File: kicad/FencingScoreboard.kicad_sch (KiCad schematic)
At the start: 6 parts, among them IC1 PIC16F18855-I-ML, J1 USB_B_Micro

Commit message: Schematic design
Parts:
- added BZ1: Buzzer, symbol Device:Buzzer
- added C1, C2, C3: 100nF, Capacitor_SMD:C_0603_1608Metric, symbol Device:C
- added ICSP: Conn_01x06_Socket, Connector_PinHeader_2.54mm:PinHeader_1x06_P2.54mm_Vertical, symbol Connector:Conn_01x06_Socket
- added J2: Conn_01x04_Socket, Connector_PinHeader_2.54mm:PinHeader_1x04_P2.54mm_Vertical, symbol Connector:Conn_01x04_Socket
- added Q1: 2N7002, Package_TO_SOT_SMD:SOT-23, symbol Transistor_FET:2N7002
- added R1: 10K, Resistor_SMD:R_0805_2012Metric, symbol Device:R
- added R2, R3: 3K6, Resistor_SMD:R_0805_2012Metric, symbol Device:R
- added R4: 1K, Resistor_SMD:R_0805_2012Metric, symbol Device:R
- IC1: footprint (none) -> Package_DFN_QFN:QFN-28-1EP_6x6mm_P0.65mm_EP4.25x4.25mm_ThermalVias
- IC2: value ~ -> TLC59281RGE
- IC3: value ~ -> TLC59281RGE; footprint (none) -> Package_DFN_QFN:QFN-28-1EP_6x6mm_P0.65mm_EP4.25x4.25mm
- J1: footprint (none) -> DMW-Custom:Molex_105164-0001_MicroUSB
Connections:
- net +5V: now also D1.18 (D3+), D1.19 (D2+), D1.26 (D1+), D2.18 (D3+), D2.19 (D2+), D2.26 (D1+), IC1.17 (VDD), IC2.21 (VCC), IC3.21 (VCC), J1.1 (VBUS), C1.1, C2.1, C3.1, ICSP.2 (Pin_2), Q1.3 (D), R1.2
- net GND: now also IC1.16 (VSS), IC1.5 (VSS), IC2.22 (GND), IC3.22 (GND), J1.5 (GND), J1.6 (Shield), BZ1.2 (+), C1.2, C2.2, C3.2, ICSP.3 (Pin_3), R2.2, R3.2, R4.1
- net at D1.11 (D3D-): now also IC2.13 (OUT11)
- net at D1.12 (D3G-): now also IC2.14 (OUT12)
- net at D1.16 (D3A-): now also IC2.12 (OUT10)
- net at D1.2 (D1D-): now also IC2.10 (OUT8)
- net at D1.20 (D2B-): now also IC2.3 (OUT1)
- net at D1.21 (D2A-): now also IC2.2 (OUT0)
- net at D1.22 (D2G-): now also IC2.8 (OUT6)
- net at D1.23 (D2F-): now also IC2.7 (OUT5)
- net at D1.25 (D1A-): now also IC2.9 (OUT7)
- net at D1.28 (D1G-): now also IC2.11 (OUT9)
- net at D1.6 (D2E-): now also IC2.6 (OUT4)
- net at D1.7 (D2D-): now also IC2.5 (OUT3)
- net at D1.8 (D2C-): now also IC2.4 (OUT2)
- net at D2.11 (D3D-): now also IC3.13 (OUT11)
- net at D2.12 (D3G-): now also IC3.14 (OUT12)
- net at D2.16 (D3A-): now also IC3.12 (OUT10)
- net at D2.2 (D1D-): now also IC3.10 (OUT8)
- net at D2.20 (D2B-): now also IC3.3 (OUT1)
- net at D2.21 (D2A-): now also IC3.2 (OUT0)
- net at D2.22 (D2G-): now also IC3.8 (OUT6)
- net at D2.23 (D2F-): now also IC3.7 (OUT5)
- net at D2.25 (D1A-): now also IC3.9 (OUT7)
- net at D2.28 (D1G-): now also IC3.11 (OUT9)
- net at D2.6 (D2E-): now also IC3.6 (OUT4)
- net at D2.7 (D2D-): now also IC3.5 (OUT3)
- net at D2.8 (D2C-): now also IC3.4 (OUT2)
- net at IC1.1 (RA2): now also IC2.1 (LAT)
- net at IC1.10 (RC2): now also J2.3 (Pin_3)
- net at IC1.11 (RC3): now also J2.4 (Pin_4)
- net at IC1.18 (RB0): now also Q1.1 (G)
- net at IC1.2 (RA3): now also IC3.1 (LAT)
- net at IC1.24 (ICSPCLK/RB6): now also ICSP.5 (Pin_5)
- net at IC1.25 (ISCPDAT/RB7): now also ICSP.4 (Pin_4)
- net at IC1.26 (RE3/~{MCLR}/VPP): now also ICSP.1 (Pin_1), R1.1
- net at IC1.27 (RA0): now also IC2.24 (SCLK), IC3.24 (SCLK)
- net at IC1.28 (RA1): now also IC2.23 (SIN), IC3.23 (SIN)
- net at IC1.8 (RC0): now also J2.1 (Pin_1)
- net at IC1.9 (RC1): now also J2.2 (Pin_2)
- net at IC2.20 (IREF): now also R2.1
- net at IC3.20 (IREF): now also R3.1
- new net: BZ1.1 (-), Q1.2 (S), R4.2

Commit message: PCB development
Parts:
- BZ1: footprint (none) -> Buzzer_Beeper:Buzzer_12x9.5RM7.6
- D1, D2: footprint (none) -> DMW-Custom:LDT-x51xRI
- IC2: footprint (none) -> Package_DFN_QFN:QFN-24-1EP_4x4mm_P0.5mm_EP2.15x2.15mm_ThermalVias
- IC3: footprint Package_DFN_QFN:QFN-28-1EP_6x6mm_P0.65mm_EP4.25x4.25mm -> Package_DFN_QFN:QFN-24-1EP_4x4mm_P0.5mm_EP2.15x2.15mm_ThermalVias
- renumbered ICSP to ICSP1
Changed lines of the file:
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@@
       (effects (font (size 1.524 1.524)))
     )
-    (property "Footprint" "" (at 138.43 143.51 0)
+    (property "Footprint" "DMW-Custom:LDT-x51xRI" (at 138.43 143.51 0)
       (effects (font (size 1.524 1.524)))
     )
@@
       (effects (font (size 1.27 1.27)))
     )
-    (property "Footprint" "Package_DFN_QFN:QFN-28-1EP_6x6mm_P0.65mm_EP4.25x4.25mm" (at 172.72 157.48 0)
+    (property "Footprint" "Package_DFN_QFN:QFN-24-1EP_4x4mm_P0.5mm_EP2.15x2.15mm_ThermalVias" (at 172.72 157.48 0)
       (effects (font (size 1.27 1.27)) hide)
     )
@@
   (symbol (lib_id "Connector:Conn_01x06_Socket") (at 146.05 76.2 0) (unit 1)
     (in_bom yes) (on_board yes) (dnp no)
-    (property "Reference" "ICSP" (at 146.05 68.58 0)
+    (property "Reference" "ICSP1" (at 146.05 68.58 0)
       (effects (font (size 1.27 1.27)))
     )
@@
       (project "FencingScoreboard"
         (path "/ffddfb19-0df0-46d6-bd3f-7efd29422964"
-          (reference "ICSP") (unit 1)
+          (reference "ICSP1") (unit 1)
         )
       )
@@
       (effects (font (size 1.524 1.524)))
     )
-    (property "Footprint" "" (at 38.1 166.37 0)
+    (property "Footprint" "DMW-Custom:LDT-x51xRI" (at 38.1 166.37 0)
       (effects (font (size 1.524 1.524)))
     )
@@
       (effects (font (size 1.27 1.27)))
     )
-    (property "Footprint" "" (at 66.04 187.96 0)
+    (property "Footprint" "Package_DFN_QFN:QFN-24-1EP_4x4mm_P0.5mm_EP2.15x2.15mm_ThermalVias" (at 66.04 187.96 0)
       (effects (font (size 1.27 1.27)) hide)
     )
@@
       (effects (font (size 1.27 1.27)) (justify left))
     )
-    (property "Footprint" "" (at 163.195 55.88 90)
-      (effects (font (size 1.27 1.27)) hide)
-    )
+    (property "Footprint" "Buzzer_Beeper:Buzzer_12x9.5RM7.6" (at 163.195 55.88 90)
+      (effects (font (size 1.27 1.27)) hide)
+    )

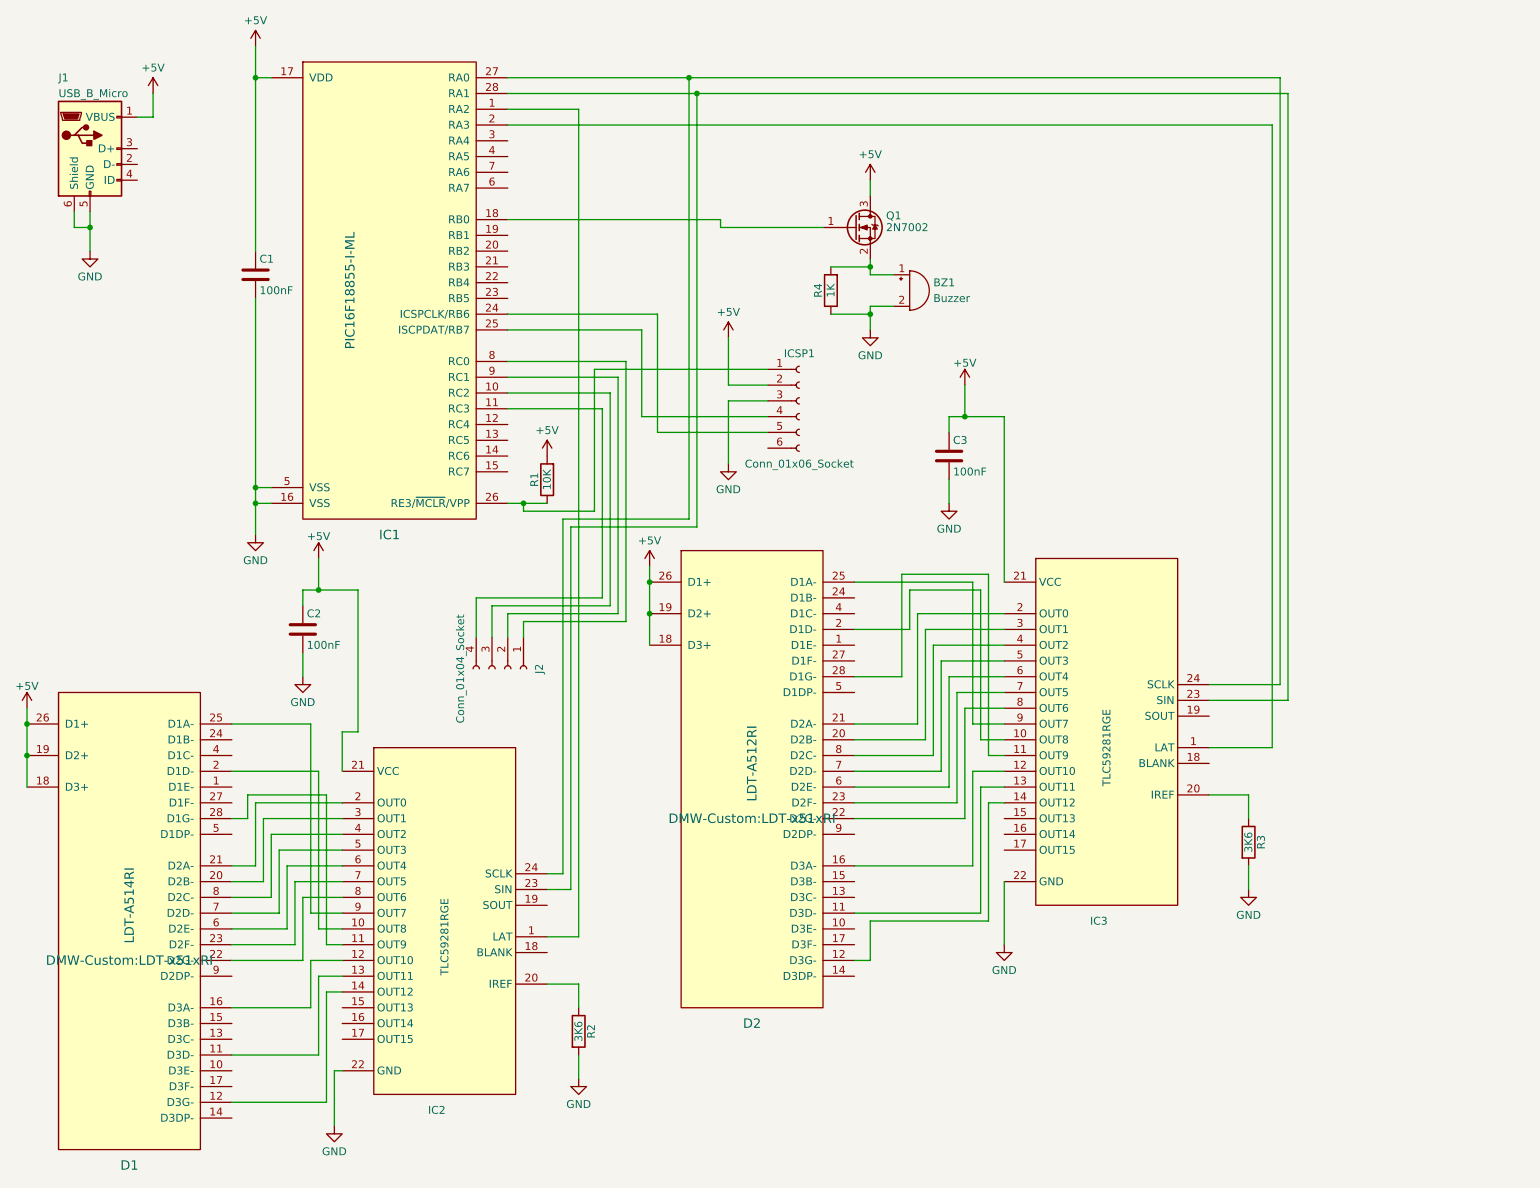
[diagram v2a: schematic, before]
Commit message: Redesign for new LED driver, route PCB
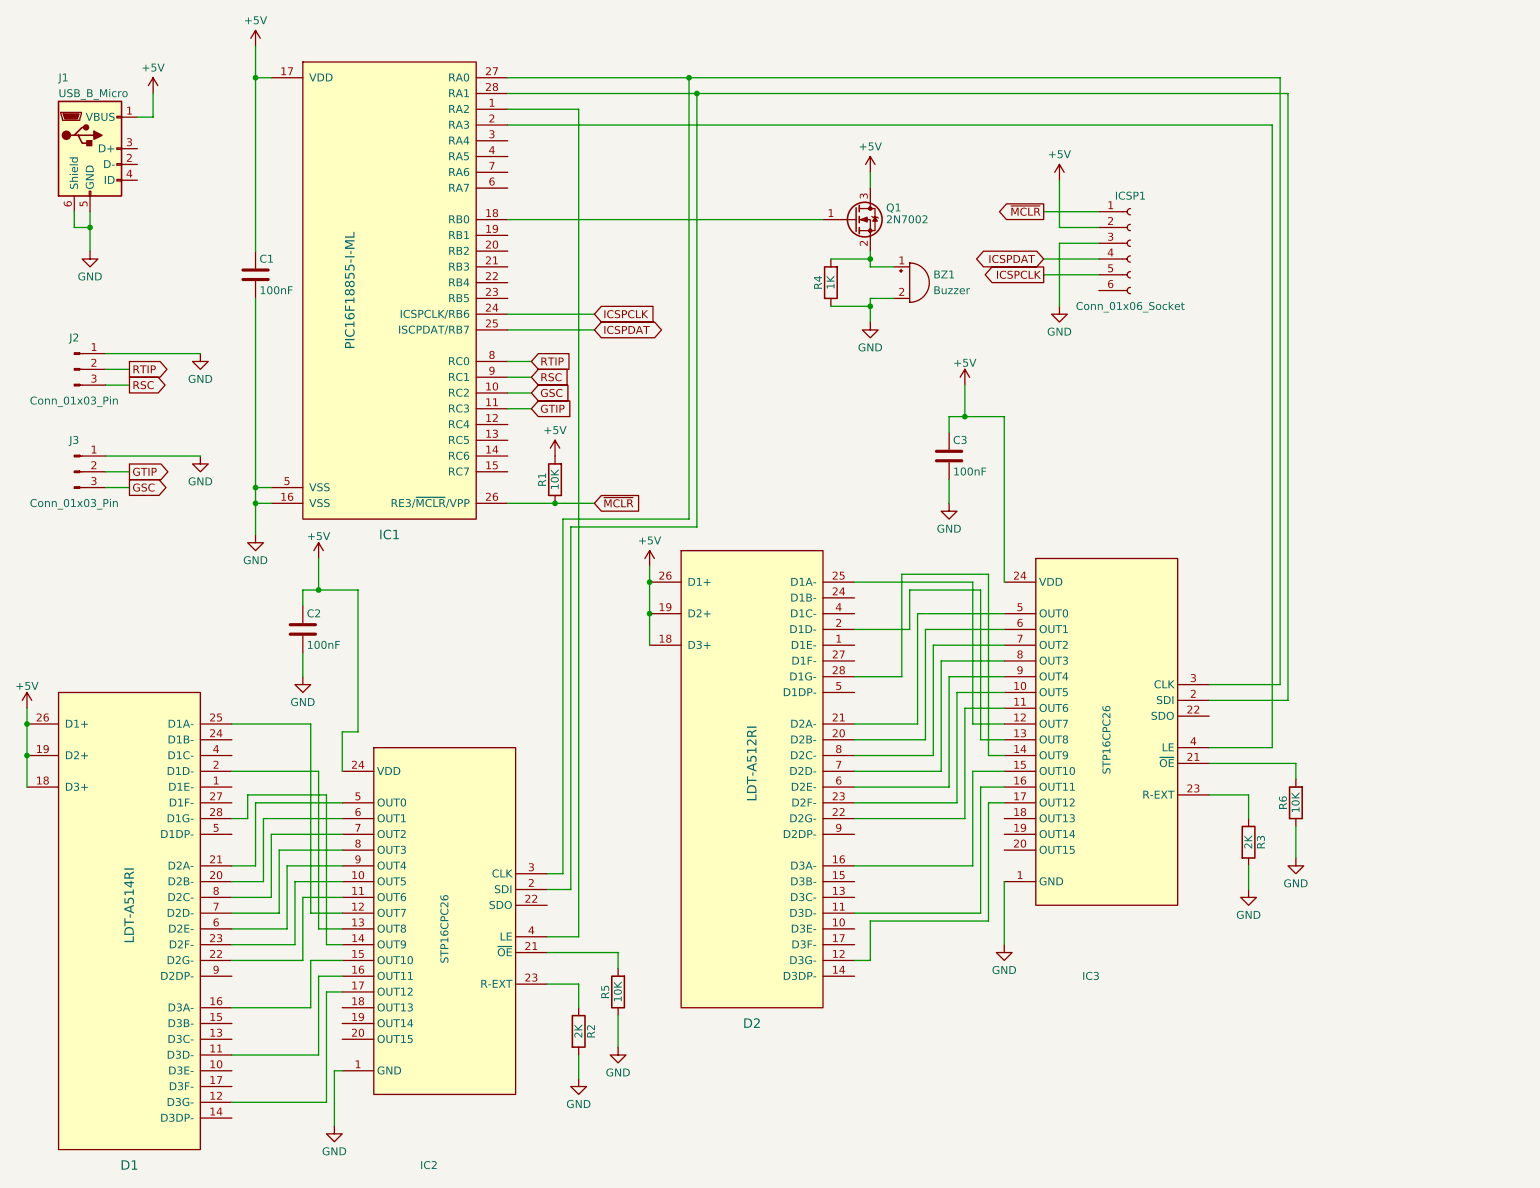
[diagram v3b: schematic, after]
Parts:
- removed IC2, IC3: TLC59281RGE, Package_DFN_QFN:QFN-24-1EP_4x4mm_P0.5mm_EP2.15x2.15mm_ThermalVias, symbol DMW-Custom:TLC59281RGE
- removed J2: Conn_01x04_Socket, Connector_PinHeader_2.54mm:PinHeader_1x04_P2.54mm_Vertical, symbol Connector:Conn_01x04_Socket
- added IC2, IC3: STP16CPC26, Package_SO:SOP-24_7.5x15.4mm_P1.27mm, symbol DMW-Custom:STP16CPC26
- added J2, J3: Conn_01x03_Pin, Connector_PinHeader_1.27mm:PinHeader_1x03_P1.27mm_Vertical, symbol Connector:Conn_01x03_Pin
- added R5, R6: 10K, Resistor_SMD:R_0805_2012Metric, symbol Device:R
- R2, R3: value 3K6 -> 2K
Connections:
- net +5V: now also IC2.24 (VDD), IC3.24 (VDD)
- net GND: now also IC2.1 (GND), IC3.1 (GND), J2.1 (Pin_1), J3.1 (Pin_1), R5.1, R6.1
- net at D2.11 (D3D-): now also IC3.16 (OUT11)
- net at D2.12 (D3G-): now also IC3.17 (OUT12)
- net at D2.16 (D3A-): now also IC3.15 (OUT10)
- net at D2.2 (D1D-): now also IC3.13 (OUT8)
- net at D2.20 (D2B-): now also IC3.6 (OUT1)
- net at D2.21 (D2A-): now also IC3.5 (OUT0)
- net at D2.22 (D2G-): now also IC3.11 (OUT6)
- net at D2.23 (D2F-): now also IC3.10 (OUT5)
- net at D2.25 (D1A-): now also IC3.12 (OUT7)
- net at D2.28 (D1G-): now also IC3.14 (OUT9)
- net at D2.6 (D2E-): now also IC3.9 (OUT4)
- net at D2.7 (D2D-): now also IC3.8 (OUT3)
- net at D2.8 (D2C-): now also IC3.7 (OUT2)
- net at IC1.2 (RA3): now also IC3.4 (LE)
- net at R3.1: now also IC3.23 (R-EXT)
- net at IC1.28 (RA1): now also IC2.2 (SDI), IC3.2 (SDI)
- net at IC1.27 (RA0): now also IC2.3 (CLK), IC3.3 (CLK)
- net ~{MCLR}: now reaches IC1.26 (RE3/~{MCLR}/VPP), ICSP1.1 (Pin_1), R1.1
- net ICSPDAT: now reaches IC1.25 (ISCPDAT/RB7), ICSP1.4 (Pin_4)
- net ICSPCLK: now reaches IC1.24 (ICSPCLK/RB6), ICSP1.5 (Pin_5)
- net RTIP: now reaches IC1.8 (RC0)
- net RTIP: now also J2.2 (Pin_2)
- net RSC: now reaches IC1.9 (RC1)
- net RSC: now also J2.3 (Pin_3)
- net GSC: now reaches IC1.10 (RC2)
- net GSC: now also J3.3 (Pin_3)
- net GTIP: now reaches IC1.11 (RC3)
- net GTIP: now also J3.2 (Pin_2)
- net at D1.11 (D3D-): now also IC2.16 (OUT11)
- net at D1.12 (D3G-): now also IC2.17 (OUT12)
- net at D1.16 (D3A-): now also IC2.15 (OUT10)
- net at D1.2 (D1D-): now also IC2.13 (OUT8)
- net at D1.20 (D2B-): now also IC2.6 (OUT1)
- net at D1.21 (D2A-): now also IC2.5 (OUT0)
- net at D1.22 (D2G-): now also IC2.11 (OUT6)
- net at D1.23 (D2F-): now also IC2.10 (OUT5)
- net at D1.25 (D1A-): now also IC2.12 (OUT7)
- net at D1.28 (D1G-): now also IC2.14 (OUT9)
- net at D1.6 (D2E-): now also IC2.9 (OUT4)
- net at D1.7 (D2D-): now also IC2.8 (OUT3)
- net at D1.8 (D2C-): now also IC2.7 (OUT2)
- net at IC1.1 (RA2): now also IC2.4 (LE)
- net at R2.1: now also IC2.23 (R-EXT)
- new net: IC2.21 (~{OE}), R5.2
- new net: IC3.21 (~{OE}), R6.2
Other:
- company: David's Makerworks -> David's MakerWorks
- title: Fencing Scoreboard -> Fencing Hit Indicator with Score Display
- moved on the sheet: BZ1, ICSP1, Q1, R1, R4

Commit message: Update design rules, remove thermal vias
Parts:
- IC1: footprint Package_DFN_QFN:QFN-28-1EP_6x6mm_P0.65mm_EP4.25x4.25mm_ThermalVias -> Package_DFN_QFN:QFN-28-1EP_6x6mm_P0.65mm_EP4.25x4.25mm
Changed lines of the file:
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@@
       (effects (font (size 1.524 1.524)))
     )
-    (property "Footprint" "Package_DFN_QFN:QFN-28-1EP_6x6mm_P0.65mm_EP4.25x4.25mm_ThermalVias" (at 80.01 58.42 0)
+    (property "Footprint" "Package_DFN_QFN:QFN-28-1EP_6x6mm_P0.65mm_EP4.25x4.25mm" (at 80.01 58.42 0)
       (effects (font (size 1.524 1.524)) hide)
     )
